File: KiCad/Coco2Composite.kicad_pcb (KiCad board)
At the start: 2 copper layers, 65.1 x 39.7 mm, 19 parts, among them J3 AUDIO_JACK_3.5MM_PTH, Q1 PN2907, Q2 2N2222, U1 MC1372

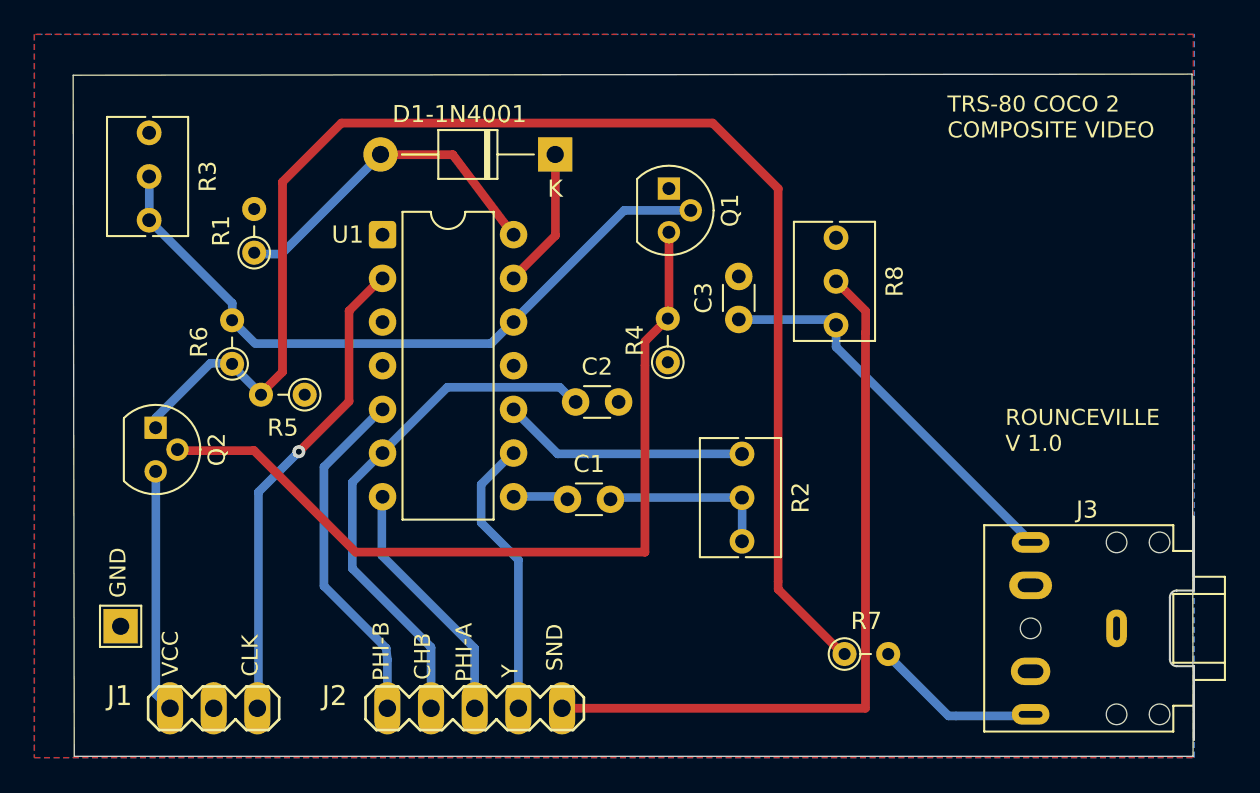
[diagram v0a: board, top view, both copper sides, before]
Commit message: Updated KiCad based on board schematic
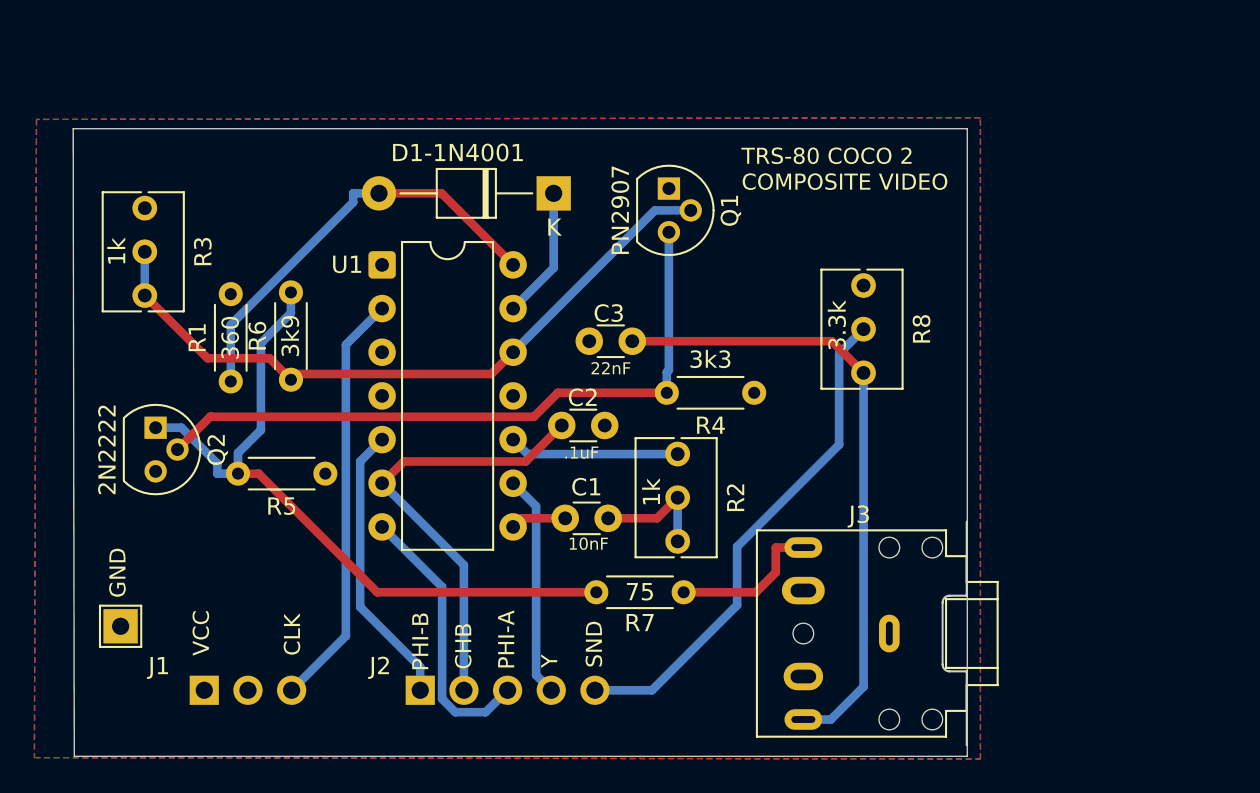
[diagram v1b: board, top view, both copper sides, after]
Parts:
- J1: value (none) -> MA03-1; footprint Coco2Composite:MA03-1_162 -> Connector_PinHeader_2.54mm:PinHeader_1x03_P2.54mm_Vertical; moved to B.Cu
- J2: value (none) -> MA05-1; footprint Coco2Composite:MA05-1_162 -> Connector_PinHeader_2.54mm:PinHeader_1x05_P2.54mm_Vertical; moved to B.Cu
- R1, R4, R5, R6, R7: footprint Resistor_THT:R_Axial_DIN0204_L3.6mm_D1.6mm_P2.54mm_Vertical -> Resistor_THT:R_Axial_DIN0204_L3.6mm_D1.6mm_P5.08mm_Horizontal
- moved R7 14.9 mm to (146.5, 115.3)
- moved J3 13.2 mm to (163.5, 117.7)
- moved R1 7.61 mm to (125.2, 103.0)
- moved C3 6.32 mm to (148.6, 100.7), turned to 180 degrees
- moved R4 5.33 mm to (155.6, 103.7), turned to 180 degrees
- moved R5 4.74 mm to (130.7, 108.4)
- moved R3 4.39 mm to (120.2, 98.0)
- moved R2 3.74 mm to (151.2, 112.3)
- moved R6 3.54 mm to (128.7, 102.9)
- moved J2 3.34 mm to (136.2, 121.0), turned to -90 degrees
- moved R8 3.21 mm to (162.0, 102.5)
- moved D1-1N4001 2.26 mm to (144.0, 92.1)
- moved U1 1.76 mm to (134.0, 96.3)
- moved C2 1.59 mm to (144.4, 105.6)
- moved J1 1.18 mm to (123.7, 121.0), turned to -90 degrees
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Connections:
- net CHB renamed Net-(U1-COL_REF_IN)
- net CLK renamed Net-(U1-OSC_IN)
- net PHIB renamed Net-(U1-COL_B_IN)
- net PHI_A renamed Net-(U1-COL_A_IN)
- net Y renamed Net-(U1-LUM_IN)
- J1 pad 2: (no net) -> unconnected-(J1-Pad2)
- J3 pad R: COMP_OUT -> SND_OUT
- J3 pad T: SND_OUT -> COMP_OUT
- Q1 pad 1: (no net) -> VCC
- Q1 pad 2: RF_OUT -> Net-(U1-RF_OUT)
- R3 pad 1: RF_OUT -> Net-(U1-RF_OUT)
- R3 pad 2: RF_OUT -> Net-(U1-RF_OUT)
- R6 pad 1: Net-(Q2-E) -> Net-(U1-RF_OUT)
- R6 pad 2: RF_OUT -> Net-(Q2-E)
- U1 pad 12: RF_OUT -> Net-(U1-RF_OUT)
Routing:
- net RF_OUT: track 41.0 -> 0.00 mm
- net Net-(Q2-E): track 82.3 -> 41.8 mm
- net Net-(U1-RF_OUT): track 0.00 -> 40.4 mm
- net VCC: track 14.1 -> 0.00 mm
- net SND: track 43.2 -> 29.4 mm
- net SND_OUT: track 23.0 -> 36.8 mm
- net Net-(Q2-B): track 48.8 -> 39.2 mm
- net Net-(U1-RF_TANK_2): track 19.8 -> 24.9 mm
- net Net-(U1-COL_REF_IN): track 30.6 -> 25.9 mm
- net Net-(U1-CHROM_IN): track 14.4 -> 9.92 mm
- net Net-(U1-COL_B_IN): track 20.3 -> 16.6 mm
- net Net-(U1-LUM_IN): track 16.5 -> 13.0 mm
- net Net-(U1-OSC_IN): track 27.9 -> 24.4 mm, vias 1 -> 0
- net Net-(C1-Pad2): track 10.1 -> 7.08 mm
- net Net-(U1-COL_A_IN): track 14.6 -> 16.1 mm
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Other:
- board size 65.1 x 39.7 mm -> 52 x 36.5 mm
- board text removed: "ROUNCEVILLE V 1.0"

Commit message: updated layout, shifted headers a tiny bit
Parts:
- moved C2 13.6 mm to (130.8, 106.2), turned to 180 degrees
- moved R1 11.8 mm to (129.7, 92.1), turned to 180 degrees
- moved R5 7.24 mm to (125.6, 113.5), turned to 90 degrees
- moved R6 1.75 mm to (128.8, 101.2), turned to 180 degrees
- moved C1 0.50 mm to (144.7, 111.5)
- moved R4 0.20 mm to (155.8, 103.7)
- moved J2 0.20 mm to (136.4, 121.0)
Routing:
- net Net-(U1-RF_TANK_2): track 24.9 -> 13.6 mm
- net Net-(Q2-E): track 41.8 -> 36.7 mm
- net Net-(U1-COL_A_IN): track 16.1 -> 14.1 mm, vias 0 -> 1
- net Net-(U1-OSC_IN): track 24.4 -> 25.7 mm
- net Net-(U1-RF_OUT): track 40.4 -> 41.6 mm
- net Net-(Q2-B): track 39.2 -> 40.3 mm
- net Net-(U1-COL_B_IN): track 16.6 -> 15.6 mm
- net COMP_OUT: track 8.88 -> 8.04 mm

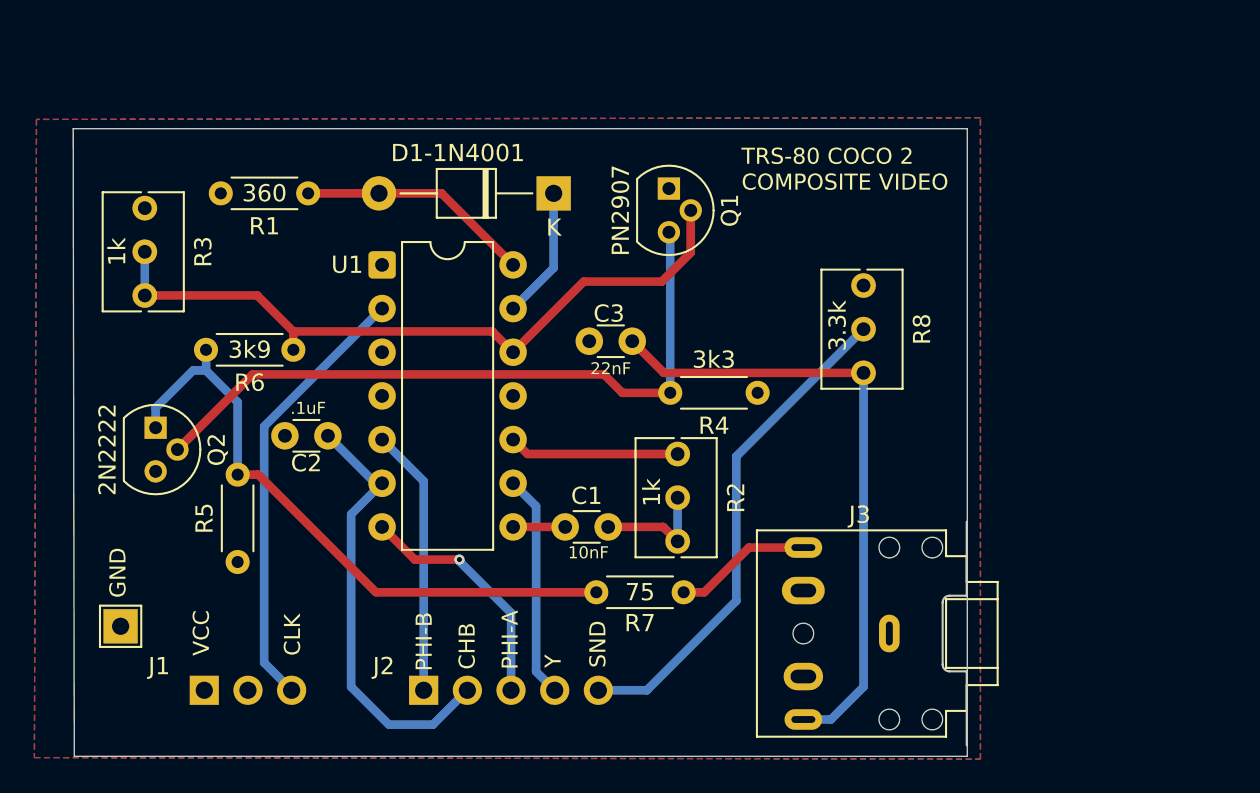
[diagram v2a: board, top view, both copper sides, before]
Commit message: updated layout to try to simplify routes
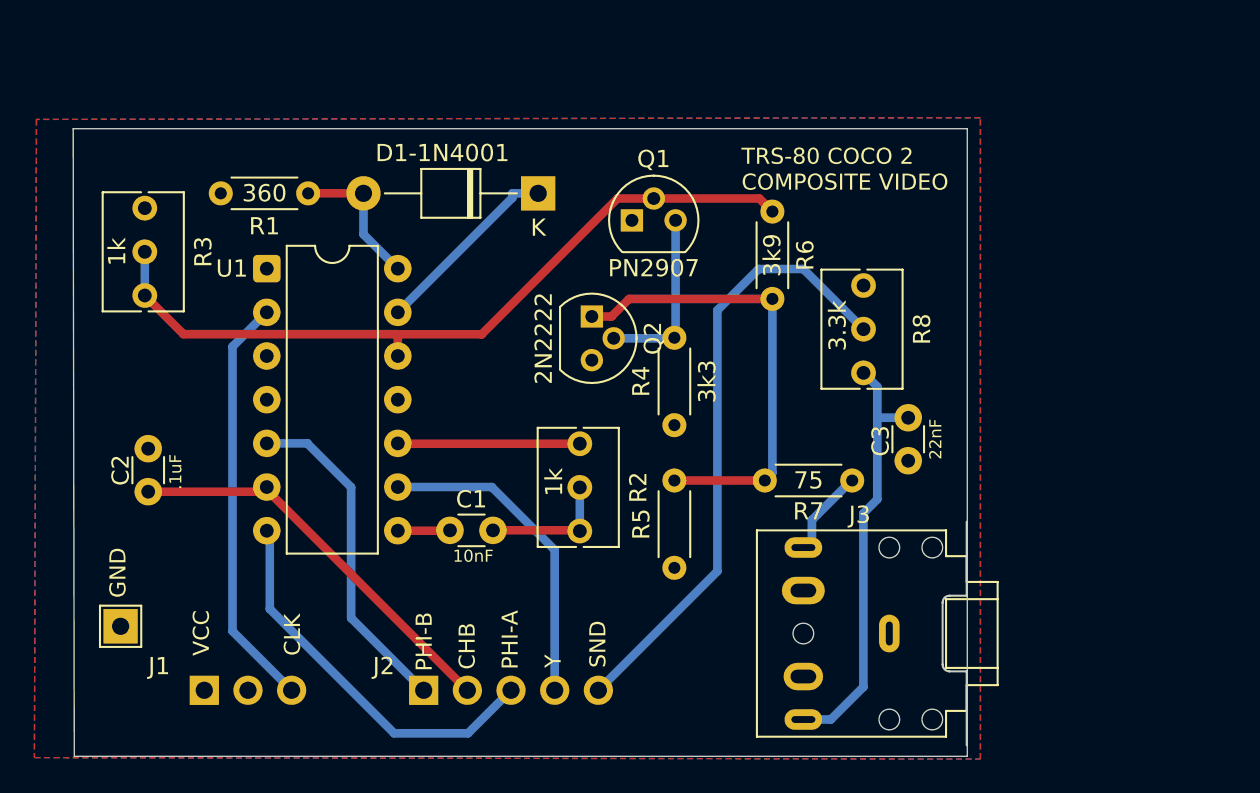
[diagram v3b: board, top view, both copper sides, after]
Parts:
- moved R6 29.0 mm to (156.7, 93.2), turned to -90 degrees
- moved Q2 26.2 mm to (146.2, 99.3)
- moved R5 25.4 mm to (151.0, 113.9)
- moved C3 16.7 mm to (164.6, 105.2), turned to -90 degrees
- moved R7 11.8 mm to (156.3, 108.8)
- moved C2 10.9 mm to (120.4, 109.5), turned to 90 degrees
- moved U1 6.71 mm to (127.3, 96.5)
- moved C1 6.70 mm to (137.9, 111.7)
- moved R2 5.72 mm to (145.5, 111.7)
- moved R4 5.19 mm to (151.0, 105.6), turned to 90 degrees
- moved Q1 2.84 mm to (148.5, 93.7), turned to 0 degrees
- moved D1-1N4001 0.90 mm to (143.1, 92.1)
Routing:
- net Net-(Q2-B): track 40.3 -> 10.4 mm
- net SND_OUT: track 36.8 -> 25.0 mm
- net Net-(Q2-E): track 36.7 -> 26.9 mm
- net Net-(U1-COL_A_IN): track 14.1 -> 22.7 mm, vias 1 -> 0
- net SND: track 29.0 -> 35.9 mm
- net Net-(U1-LUM_IN): track 13.0 -> 18.8 mm
- net Net-(U1-RF_TANK_2): track 13.6 -> 8.43 mm
- net Net-(U1-COL_B_IN): track 15.6 -> 19.5 mm
- net Net-(U1-RF_TANK_1): track 7.68 -> 11.2 mm
- net Net-(U1-RF_OUT): track 41.6 -> 44.8 mm
- net COMP_OUT: track 8.04 -> 5.39 mm
- net Net-(U1-COL_REF_IN): track 25.4 -> 23.6 mm
- net Net-(U1-OSC_IN): track 25.7 -> 24.2 mm
- net Net-(C1-Pad2): track 6.93 -> 7.61 mm
- net Net-(U1-CHROM_IN): track 9.92 -> 10.6 mm

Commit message: simplified layout & added username
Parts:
- moved R3 19.1 mm to (138.7, 102.9)
- moved U1 2.31 mm to (125.0, 96.5)
- moved C3 1.63 mm to (163.3, 106.2), turned to 0 degrees
- moved C1 1.00 mm to (136.9, 111.7)
- moved R2 0.60 mm to (144.9, 111.7)
- moved Q2 0.46 mm to (145.7, 99.3)
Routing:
- net Net-(U1-RF_OUT): track 44.8 -> 30.7 mm
- net SND: track 35.9 -> 27.4 mm
- net Net-(U1-COL_REF_IN): track 23.6 -> 27.4 mm
- net Net-(Q2-E): track 26.9 -> 29.6 mm
- net Net-(U1-COL_A_IN): track 22.7 -> 20.4 mm
- net Net-(U1-LUM_IN): track 18.8 -> 16.6 mm
- net Net-(U1-RF_TANK_1): track 11.2 -> 13.3 mm
- net Net-(U1-CHROM_IN): track 10.6 -> 12.3 mm
- net SND_OUT: track 25.0 -> 23.7 mm
- net Net-(U1-CHROM_MOD_OUT): track 3.04 -> 4.36 mm
- net Net-(U1-OSC_IN): track 24.2 -> 25.4 mm
- net Net-(U1-RF_TANK_2): track 8.43 -> 7.73 mm
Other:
- board text added: "keronian v0.1"
